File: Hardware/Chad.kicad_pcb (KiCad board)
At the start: 4 copper layers, 30 x 60 mm, 130 parts, among them J1 RBUS, J2 GPIO Breakout, J3 ServoCH0, J4 ServoCH1, J5 USB_C_Receptacle_USB2.0, Q1 SSM3K15AMFV,L3F, U1 ESP32-S3, U2 SN65HVD230, U3 LM66200DRLR, U4 MAX77827AEFD+T, U5 SC4215ASTRT, U6 SiC437AED-T1, Y1 R940000171

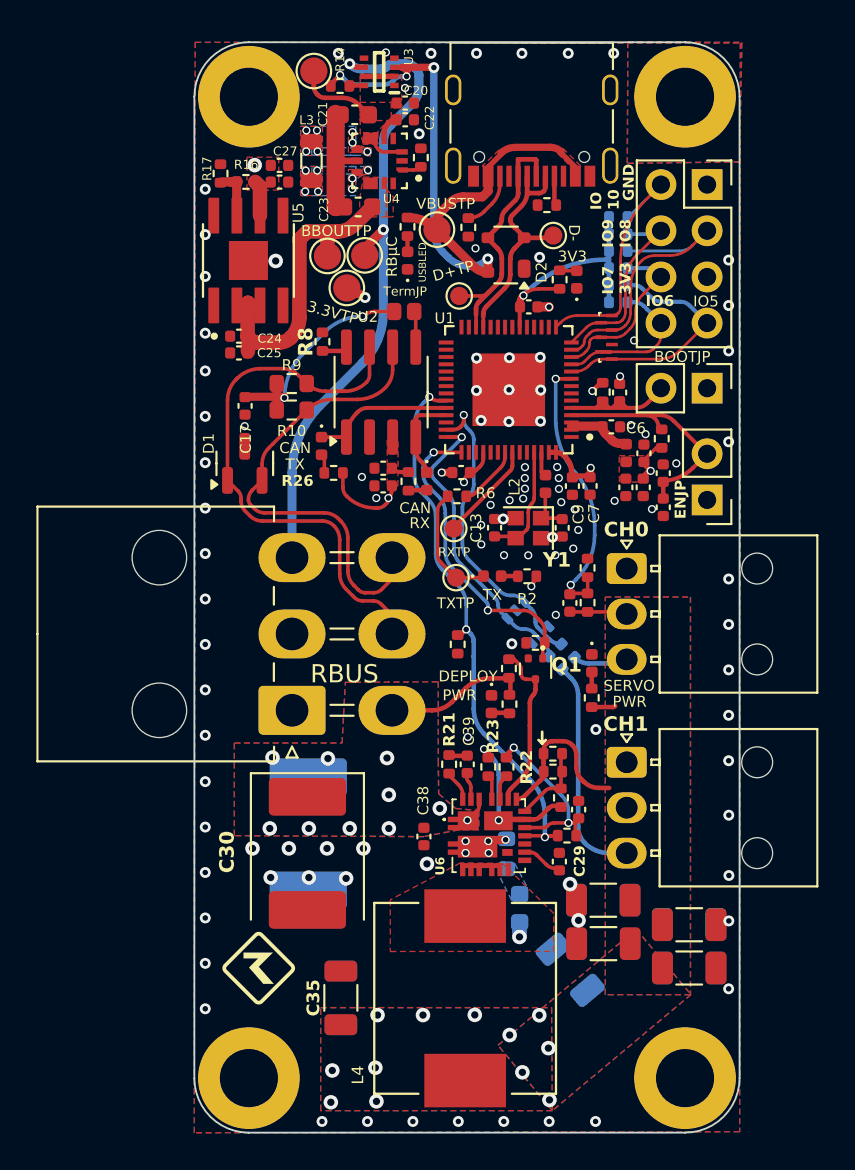
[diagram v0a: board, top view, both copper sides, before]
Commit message: updated hole size for eurocircuits
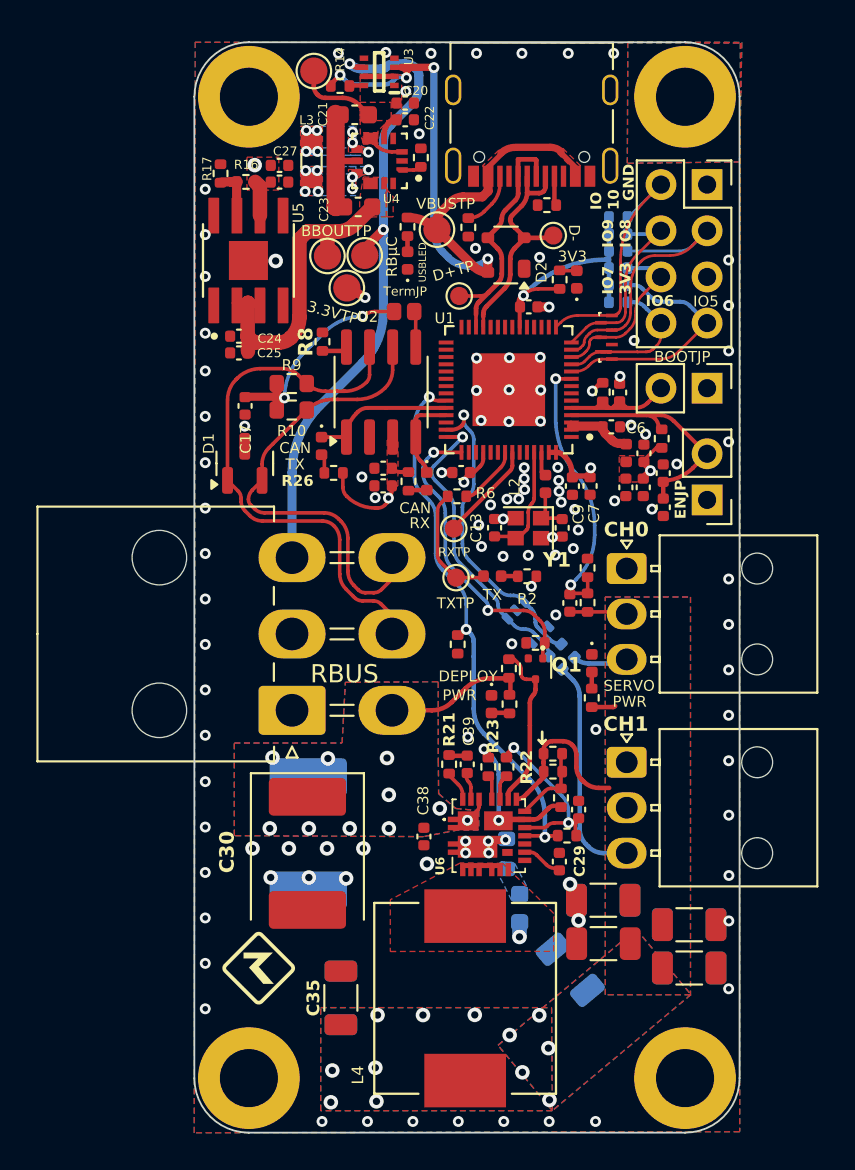
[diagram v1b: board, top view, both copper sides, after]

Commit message: cleaned up schematic and bom
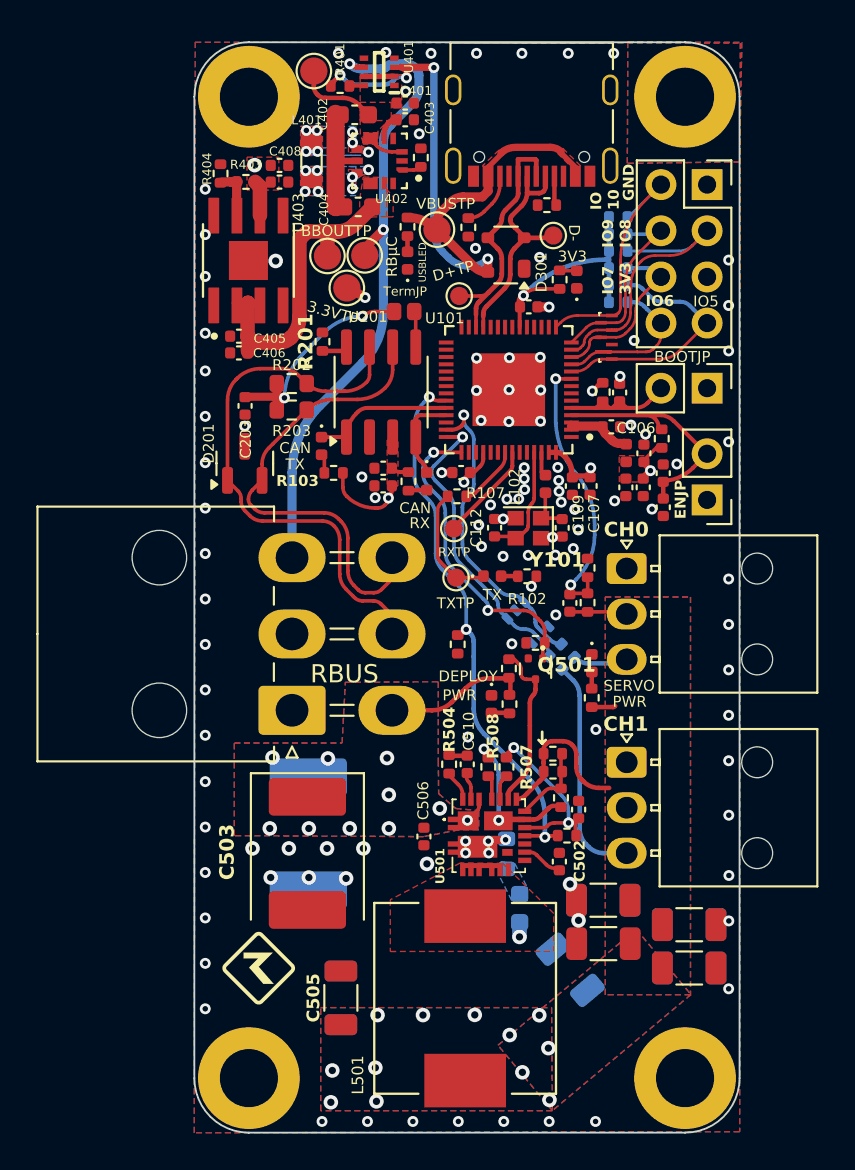
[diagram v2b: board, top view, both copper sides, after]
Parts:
- C103: renamed from C3; value 0.1uF -> 100nF
- C105: renamed from C5; value 0.1uF -> 100nF
- C106: renamed from C6; value 0.1uF -> 100nF
- C108: renamed from C8; value 0.1uF -> 100nF
- C110: renamed from C10; value 0.1uF -> 100nF
- C111: renamed from C11; value 0.1uF -> 100nF
- C114: renamed from C45; value 0.1uF -> 100nF
- C408: renamed from C27; value 0.1uF -> 100nF
- C510: renamed from C39; value 0.1uF -> 100nF
- D101: renamed from TXLED1; value GREEN_LED -> LED_GREEN
- D102: renamed from CANTXLED1; value GREEN_LED -> LED_GREEN
- D103: renamed from CANRXLED1; value AMBER_LED -> LED_ORANGE
- D104: renamed from 3V3LED1; value BLUE_LED -> LED_BLUE
- D105: renamed from 12VLED1; value RED_LED -> LED_RED
- D106: renamed from SERVOLED1; value AMBER_LED -> LED_ORANGE
- D302: renamed from USBLED1; value WHITE_LED -> LED_WHITE
- renumbered C1 to C101, C2 to C102, C4 to C104, C7 to C107, C9 to C109, C13 to C112, C14 to C113, C15 to C201, C16 to C202, C17 to C203, C20 to C401, C21 to C402, C22 to C403, C23 to C404, C24 to C405, C25 to C406, C26 to C407, C28 to C501, C29 to C502, C30 to C503, C33 to C504, C35 to C505, C38 to C506, C37 to C507, C49 to C508, C47 to C509, C18 to C511, C19 to C512, C32 to C513, C46 to C514, C48 to C515, C31 to C516, C40 to C517, D1 to D201, D2 to D301, D3 to D601, D4 to D701, H1 to H101, H2 to H102, H3 to H103, H4 to H104, ENJUMPER1 to J101, BOOTJUMPER1 to J102, J1 to J103, J5 to J301, J3 to J601, J4 to J602, J2 to J701, JP1 to JP201, L1 to L101, L2 to L102, L3 to L401, L4 to L501, Q1 to Q501, R1 to R101, R2 to R102, R26 to R103, R27 to R104, R3 to R105, R4 to R106, R6 to R107, R7 to R108, R25 to R109, R36 to R110, R37 to R111, R34 to R112, R8 to R201, R9 to R202, R10 to R203, R11 to R301, R12 to R302, R13 to R303, R14 to R401, R15 to R402, R16 to R403, R17 to R404, R18 to R501, R19 to R502, R20 to R503, R21 to R504, R39 to R505, R24 to R506, R22 to R507, R23 to R508, R38 to R509, R42 to R510, R40 to R601, R41 to R602, R28 to R701, R29 to R702, R30 to R703, R31 to R704, R32 to R705, R33 to R706, TP9 to TP101, TP10 to TP102, TP1 to TP301, TP2 to TP302, TP4 to TP401, TP5 to TP402, TP6 to TP403, TP7 to TP404, TP8 to TP405, U1 to U101, U2 to U201, U3 to U401, U4 to U402, U5 to U403, U6 to U501, Y1 to Y101

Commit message: continued
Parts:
- D601: value ~ -> CPDV5-3V3UP-HF
- L101: value 2.0nH -> 2nH
- Q501: footprint iclr:SOT-723 -> Package_TO_SOT_SMD:SOT-723
- R101, R105: value 10K -> 10kΩ
- R102, R106, R111: value 470 -> 470Ω
- R103, R104, R109, R505: value 1k -> 1kΩ
- R107: value 499 -> 499Ω
- R108: value 3k -> 3kΩ
- R110: value 1.5k -> 1.5kΩ
- R112: value 18k -> 18kΩ
- R201: value 0 -> 0Ω
- R202, R203: value 60 -> 60Ω
- R301, R302, R303: value 5.1k -> 5.1kΩ
- R401, R404, R501, R503, R509, R701, R702, R703, R704, R705, R706: value 10k -> 10kΩ
- R402: value 14k -> 14kΩ
- R403: value 56k -> 56kΩ
- R502: value 113k -> 113kΩ
- R504: value 2.2 -> 2.2Ω
- R506: value 442k -> 442kΩ
- R507: value 200k -> 200kΩ
- R508: value 100k -> 100kΩ
- R510: value 5.1R -> 5.1Ω
- R601, R602: value 165R -> 165Ω
- U501: value SiC437AED-T1 -> SIC437AED-T1-GE3
- Y101: value R940000171 -> 40MHz±10ppm; footprint iclr:Crystal_SMD_2016-4Pin_2.0x1.6mm -> Crystal:Crystal_SMD_2016-4Pin_2.0x1.6mm
- moved C112 0.12 mm to (48.4, 68.8)
- moved C113 0.11 mm to (52.4, 68.8)
